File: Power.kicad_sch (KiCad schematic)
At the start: 88 parts, among them Q3 FDMC510P, U1 ZXCT1009F, U33 TPS82150, U34 LT3097, U35 LT8582

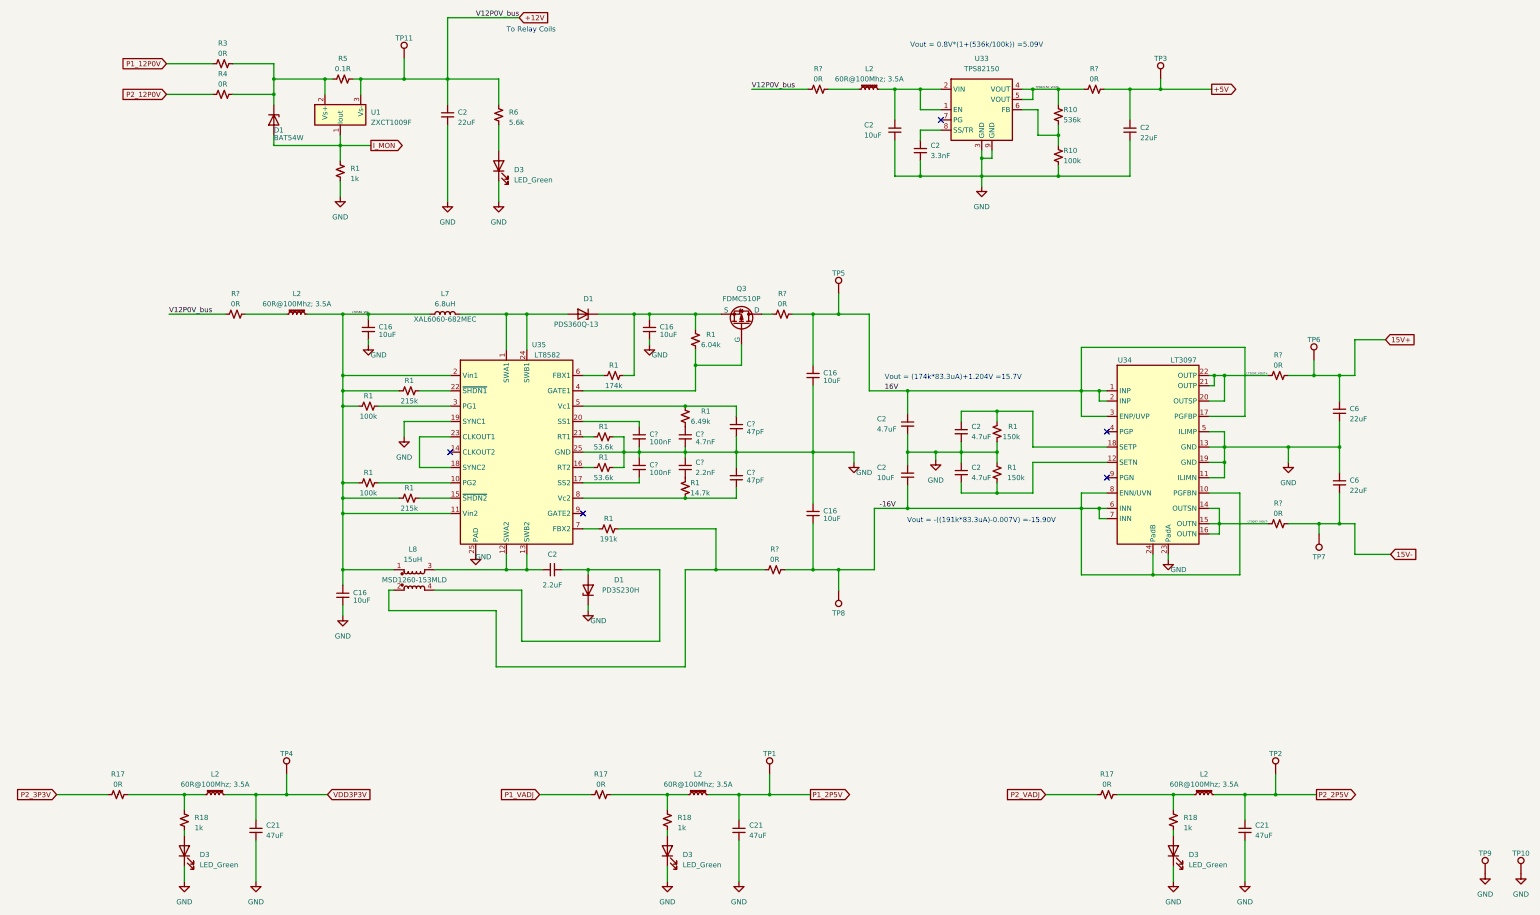
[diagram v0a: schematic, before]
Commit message: Opened & Saved Project in Kicad 9
- Opened & Saved Project in Kicad 9
- Added .gitignore from main
- Added sym-lib-table to link the unchanged symbol libs to the project
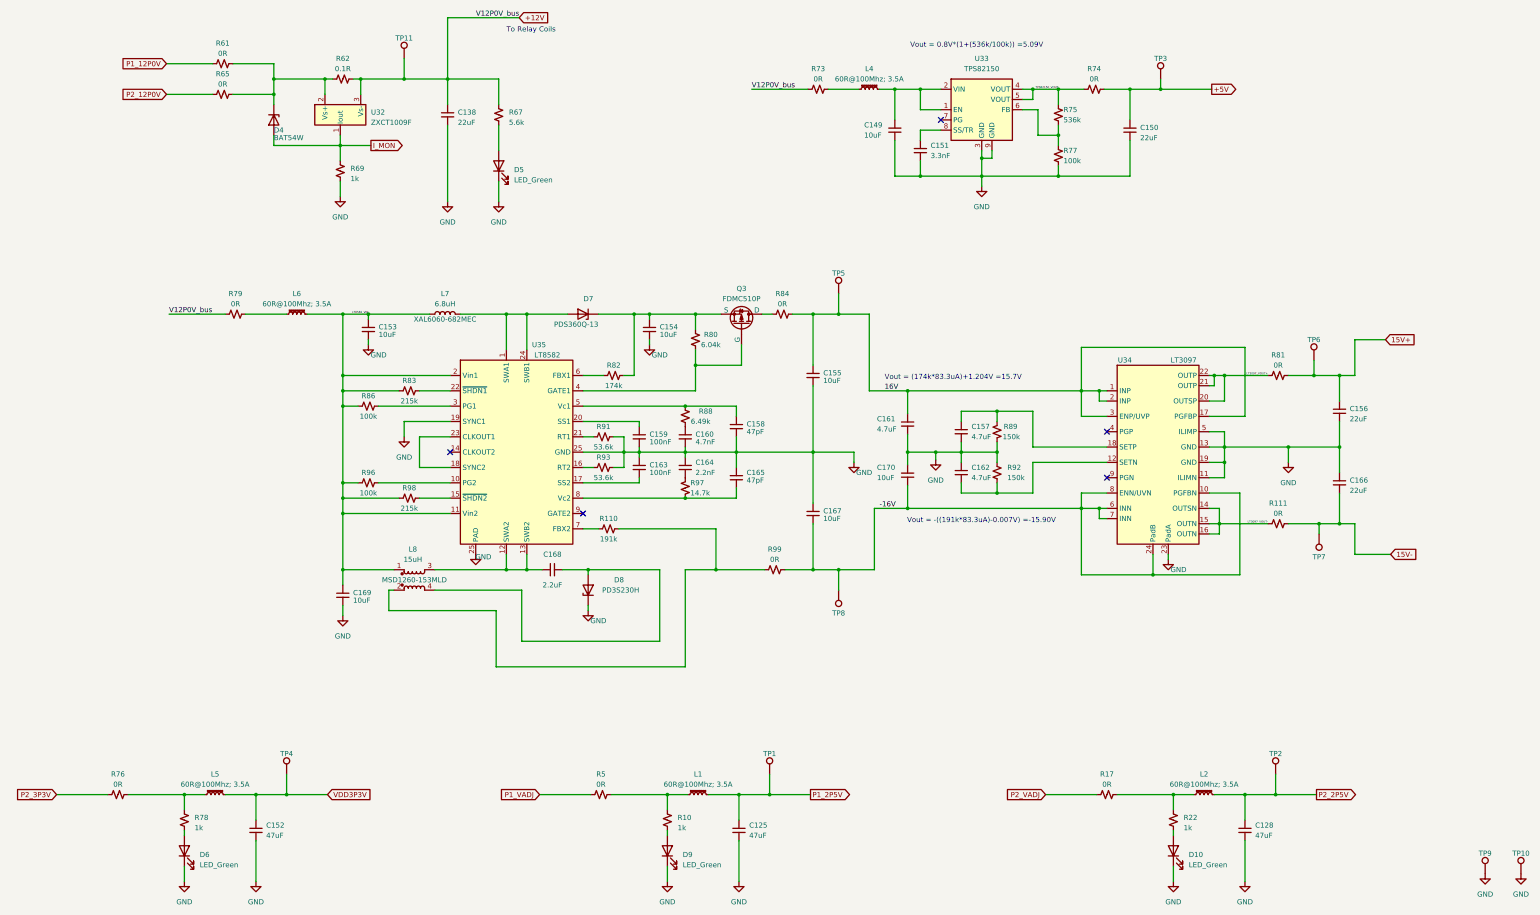
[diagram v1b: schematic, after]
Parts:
- gave numbers to parts that had none: 13
- renumbered C21 to C125, C21 to C128, C2 to C138, C2 to C149, C2 to C150, C2 to C151, C21 to C152, C16 to C153, C16 to C154, C16 to C155, C6 to C156, C2 to C157, C2 to C161, C2 to C162, C6 to C166, C16 to C167, C2 to C168, C16 to C169, C2 to C170, D3 to D10, D1 to D4, D3 to D5, D3 to D6, D1 to D7, D1 to D8, D3 to D9, L2 to L1, L2 to L4, L2 to L5, L2 to L6, R18 to R10, R1 to R110, R18 to R22, R17 to R5, R3 to R61, R5 to R62, R4 to R65, R6 to R67, R1 to R69, R10 to R75, R17 to R76, R10 to R77, R18 to R78, R1 to R80, R1 to R82, R1 to R83, R1 to R86, R1 to R88, R1 to R89, R1 to R91, R1 to R92, R1 to R93, R1 to R96, R1 to R97, R1 to R98, U1 to U32

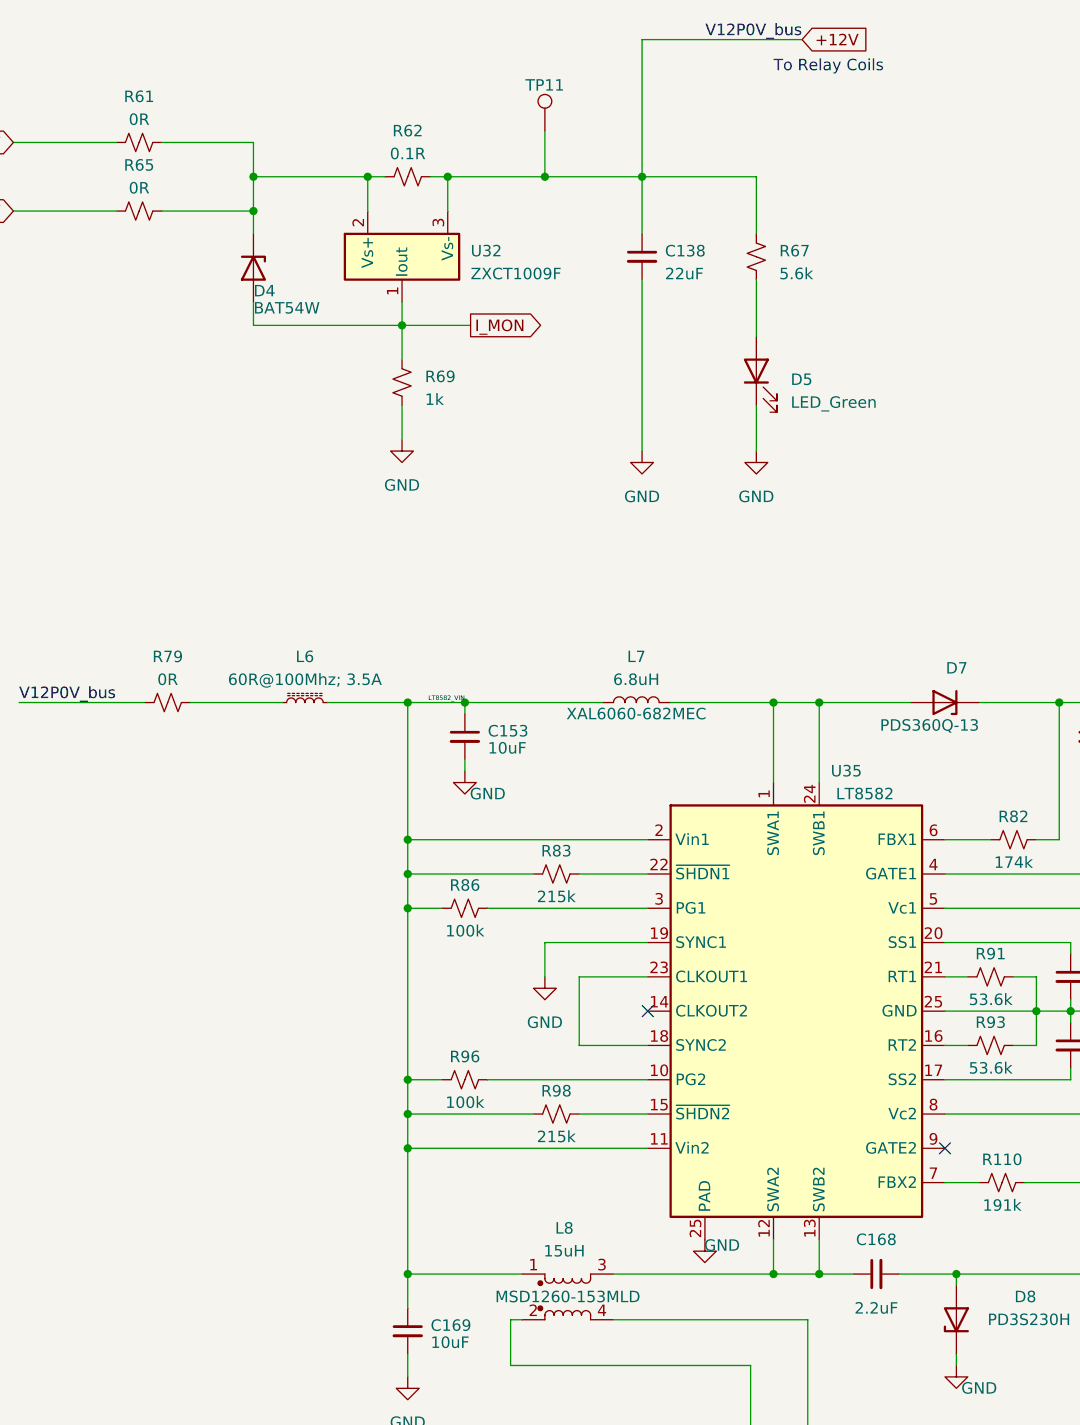
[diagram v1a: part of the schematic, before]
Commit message: Fixed Serveral ERC errors
Fixed Several ERC errors
- Ignored off-grid connections errors

- Updated a number of symbols from the Kicad default library. This should have no visual change
  - Power:Ground
  - Power:Earth
  - Device:LED

- Relinked some symbols with a new copy in the AD7688_Digitaizer_SLib. This was to fix errors/warnings where local schematic changes were made. This process was opening the local symbol; saving a copy in the AD7688_Digitaizer_SLib; relinking the part to the new part in the AD7688_Digitaizer_SLib. This should have caused no visual change.
  - EC2-12TNU relays parts (K101 etc.)
  - U36 TL071
  - U16 SI5330 (had local edit to add pin25-gnd pad)
  - U32 TXU101

- Changed D4 symbol to explicitly show the unused pin on the schematic (was an error)

- Removed an extra pin 25 from U35 showing the pad connection. Renamed the pin for clarity
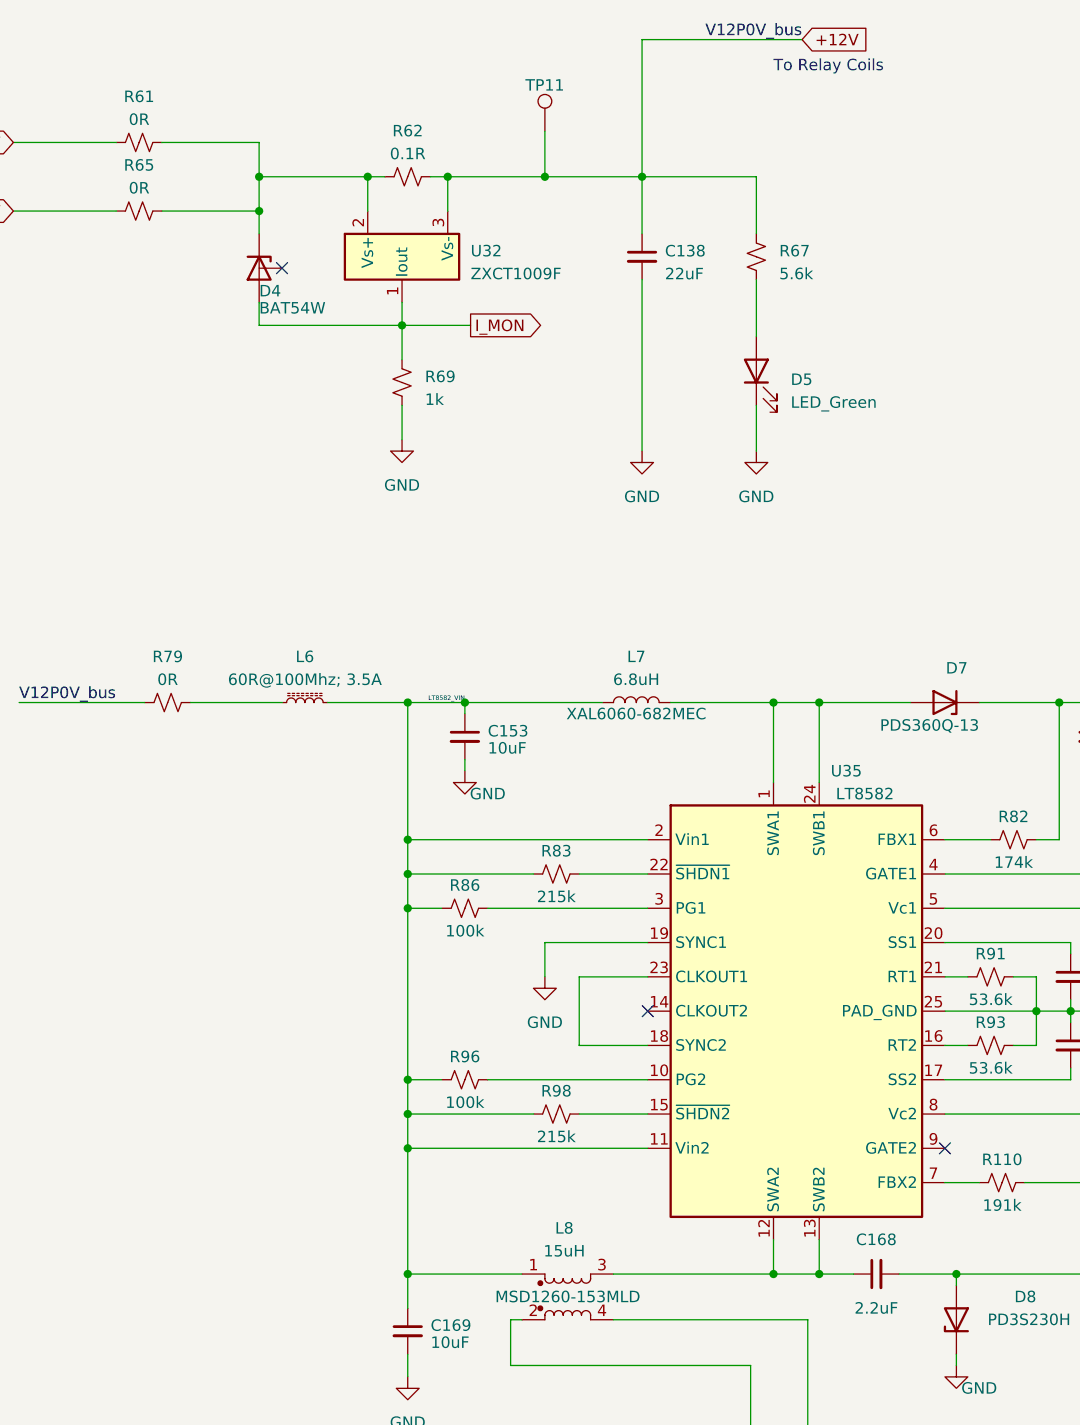
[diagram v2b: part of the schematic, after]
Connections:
- no-connect marks 5 -> 6
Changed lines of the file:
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@@
 	)
 	(junction
-		(at 84.455 36.83)
+		(at 85.09 36.83)
 		(diameter 0)
 		(color 0 0 0 0)
@@
 	)
 	(junction
-		(at 84.455 40.64)
-		(diameter 0)
-		(color 0 0 0 0)
-	)
-	(junction
 		(at 224.79 95.25)
 		(diameter 0)
@@
 	)
 	(junction
+		(at 85.09 40.64)
+		(diameter 0)
+		(color 0 0 0 0)
+	)
+	(junction
 		(at 147.32 95.25)
 		(diameter 0)
@@
 	)
 	(no_connect
+		(at 87.63 46.99)
+	)
+	(no_connect
 		(at 250.19 46.99)
 	)
@@
 	(wire
 		(pts
-			(xy 84.455 36.83) (xy 97.155 36.83)
+			(xy 85.09 36.83) (xy 97.155 36.83)
 		)
 		(stroke
@@
 	(wire
 		(pts
-			(xy 84.455 53.34) (xy 100.965 53.34)
+			(xy 85.09 53.34) (xy 100.965 53.34)
 		)
 		(stroke
@@
 	(wire
 		(pts
-			(xy 84.455 40.64) (xy 84.455 43.18)
+			(xy 85.09 40.64) (xy 85.09 43.18)
 		)
 		(stroke
@@
 	(wire
 		(pts
-			(xy 84.455 36.83) (xy 84.455 40.64)
+			(xy 85.09 36.83) (xy 85.09 40.64)
 		)
 		(stroke
@@
 	(wire
 		(pts
-			(xy 84.455 50.8) (xy 84.455 53.34)
+			(xy 85.09 50.8) (xy 85.09 53.34)
 		)
 		(stroke
@@
 	(wire
 		(pts
-			(xy 74.295 33.02) (xy 84.455 33.02)
+			(xy 74.295 33.02) (xy 85.09 33.02)
 		)
 		(stroke
@@
 	(wire
 		(pts
-			(xy 84.455 33.02) (xy 84.455 36.83)
+			(xy 85.09 33.02) (xy 85.09 36.83)
 		)
 		(stroke
@@
 	(wire
 		(pts
-			(xy 84.455 40.64) (xy 74.295 40.64)
+			(xy 74.295 40.64) (xy 85.09 40.64)
 		)
 		(stroke
@@
 	)
 	(symbol
-		(lib_id "power:GND")
-		(at 134.62 154.94 0)
-		(unit 1)
-		(exclude_from_sim no)
-		(in_bom yes)
-		(on_board yes)
-		(dnp no)
-		(property "Reference" "#PWR0101"
-			(at 134.62 161.29 0)
-			(effects
-				(font
-					(size 1.27 1.27)
-				)
-				(hide yes)
-			)
-		)
-		(property "Value" "GND"
-			(at 136.525 155.575 0)
-			(effects
-				(font
-					(size 1.27 1.27)
-				)
-			)
-		)
-		(property "Footprint" ""
-			(at 134.62 154.94 0)
-			(effects
-				(font
-					(size 1.27 1.27)
-				)
-				(hide yes)
-			)
-		)
-		(property "Datasheet" ""
-			(at 134.62 154.94 0)
-			(effects
-				(font
-					(size 1.27 1.27)
-				)
-				(hide yes)
-			)
-		)
-		(property "Description" ""
-			(at 134.62 154.94 0)
-			(effects
-				(font
-					(size 1.27 1.27)
-				)
-				(hide yes)
-			)
-		)
-		(pin "1"
-		)
-		(instances
-			(project "Zest_MPEX_v1p3"
-				(path "/00cb7cb7-8be2-4970-8959-a06932b2fa76/bd960755-3e45-476f-84b6-fdf0c21cce40"
-					(reference "#PWR020")
-					(unit 1)
-				)
-			)
-			(project "Quartz_v1p2"
-				(path "/674e1e7f-67ba-4e85-a926-dcd5f6a22021/ac1e64b2-1a26-4ac8-9188-8b2d840a4cd2"
-					(reference "#PWR0101")
-					(unit 1)
-				)
-			)
-		)
-	)
-	(symbol
 		(lib_id "Device:C_Small")
 		(at 255.27 134.62 0)
@@
 	(symbol
 		(lib_id "AD7768_Digitizer_SLib:D_BAT54W")
-		(at 84.455 46.99 270)
+		(at 85.09 46.99 270)
 		(unit 1)
 		(exclude_from_sim no)
@@
 		(dnp no)
 		(property "Reference" "D4"
-			(at 84.455 49.53 90)
+			(at 85.09 49.53 90)
 			(effects
 				(font
@@
 		)
 		(property "Value" "BAT54W"
-			(at 84.455 51.435 90)
+			(at 85.09 51.435 90)
 			(effects
 				(font
@@
 		)
 		(property "Footprint" "Package_TO_SOT_SMD:SOT-323_SC-70"
-			(at 84.455 46.99 0)
+			(at 85.09 46.99 0)
 			(effects
 				(font
@@
 		)
 		(property "Datasheet" "~"
-			(at 84.455 46.99 0)
+			(at 85.09 46.99 0)
 			(effects
 				(font
@@
 		)
 		(property "Description" ""
-			(at 84.455 46.99 0)
+			(at 85.09 46.99 0)
 			(effects
 				(font
@@
 		)
 		(property "MPN" "BAT54W-7-F"
-			(at 84.455 46.99 90)
+			(at 85.09 46.99 90)
 			(effects
 				(font
@@
 		)
 		(pin "25"
-		)
-		(pin "25"
